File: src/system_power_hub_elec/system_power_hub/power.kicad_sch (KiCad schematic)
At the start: 37 parts, among them J1 XT90M, U220 MP2459GJ-Z-MS, U230 AP62200TWU, U240 HX4002

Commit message: Draft SPM PCB layout
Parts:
- J1: value XT90M -> XT60M; footprint Connector_AMASS:AMASS_XT90PW-M_1x02_P10.90mm_Horizontal -> Connector_AMASS:AMASS_XT60IPW-M_1x03_P7.20mm_Horizontal
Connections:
- net GND: now also J1.1 (Pin_1); no longer J1.2 (Pin_2)
- net VBUS: now also J1.2 (Pin_2); no longer J1.1 (Pin_1)
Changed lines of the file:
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@@
 	(symbol
 		(lib_id "Connector:Conn_01x02_Pin")
-		(at 30.48 29.21 0)
+		(at 30.48 31.75 0)
+		(mirror x)
 		(unit 1)
 		(exclude_from_sim no)
@@
 		(dnp no)
 		(property "Reference" "J1"
-			(at 27.178 29.21 0)
+			(at 27.178 31.75 0)
 			(effects
 				(font
@@
 			)
 		)
-		(property "Value" "XT90M"
-			(at 25.908 32.512 0)
+		(property "Value" "XT60M"
+			(at 25.908 28.448 0)
 			(effects
 				(font
@@
 			)
 		)
-		(property "Footprint" "Connector_AMASS:AMASS_XT90PW-M_1x02_P10.90mm_Horizontal"
-			(at 30.48 29.21 0)
+		(property "Footprint" "Connector_AMASS:AMASS_XT60IPW-M_1x03_P7.20mm_Horizontal"
+			(at 30.48 31.75 0)
 			(effects
 				(font
@@
 		)
 		(property "Datasheet" "~"
-			(at 30.48 29.21 0)
+			(at 30.48 31.75 0)
 			(effects
 				(font
@@
 		)
 		(property "Description" "Generic connector, single row, 01x02, script generated"
-			(at 30.48 29.21 0)
+			(at 30.48 31.75 0)
 			(effects
 				(font

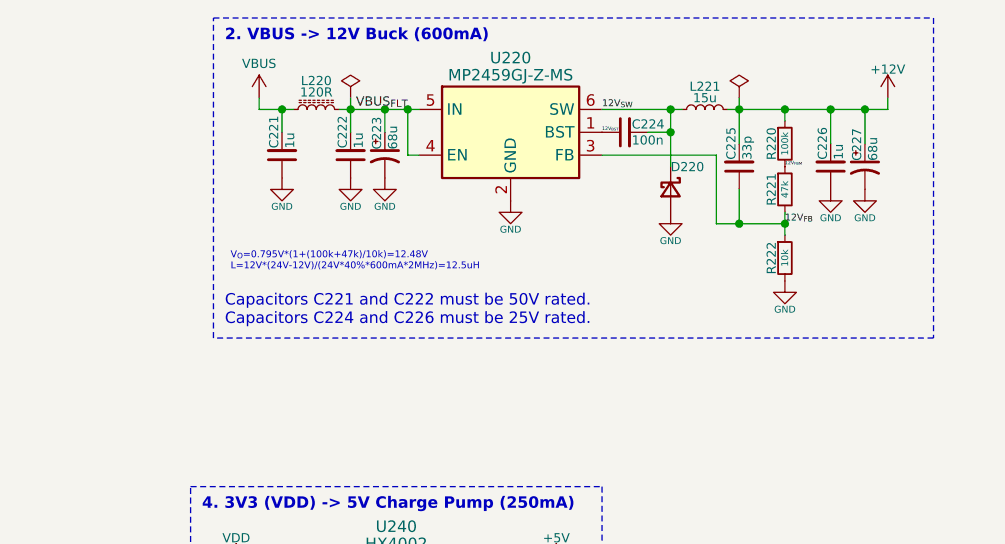
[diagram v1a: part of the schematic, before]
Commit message: Fixed XT connector routing, rewired power stuff (attempted to), made board smaller, more routing/layout progress
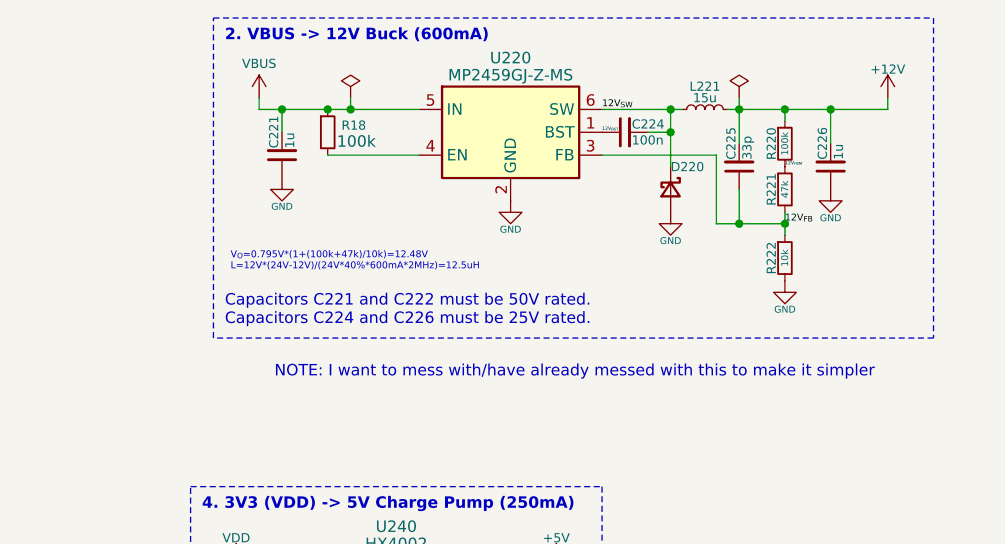
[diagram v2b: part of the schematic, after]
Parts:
- removed C222: 1u, Capacitor_SMD:C_1206_3216Metric, symbol Bluesat:C_CompactV
- removed C223, C227: 68u, Capacitor_SMD:CP_Elec_6.3x7.7, symbol Device:C_Polarized_Small_US
- removed L220: 120R, Resistor_SMD:R_0603_1608Metric, symbol Device:L_Ferrite_Small
- added R18: 100k, Resistor_SMD:R_0402_1005Metric, symbol Device:R_Small
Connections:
- net VBUS: now also U220.5 (IN), R18.1
- net VBUS_{FLT}: no longer names the net of U220.4 (EN)
- net VBUS_{FLT}: now also R18.2; no longer U220.5 (IN)
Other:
- note added: "NOTE: I want to mess with/have already messed with this to make it simpler"

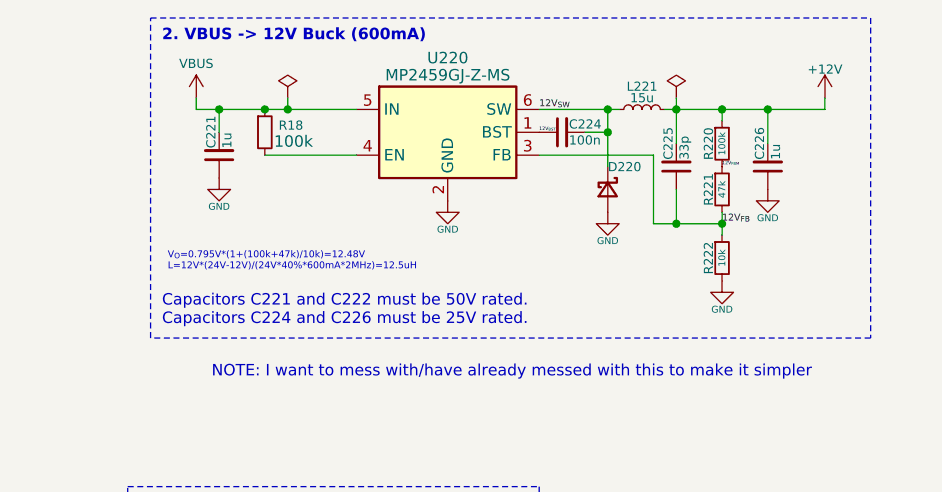
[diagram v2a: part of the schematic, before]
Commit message: Draft layout done, need to continue routing and decide on GPIO
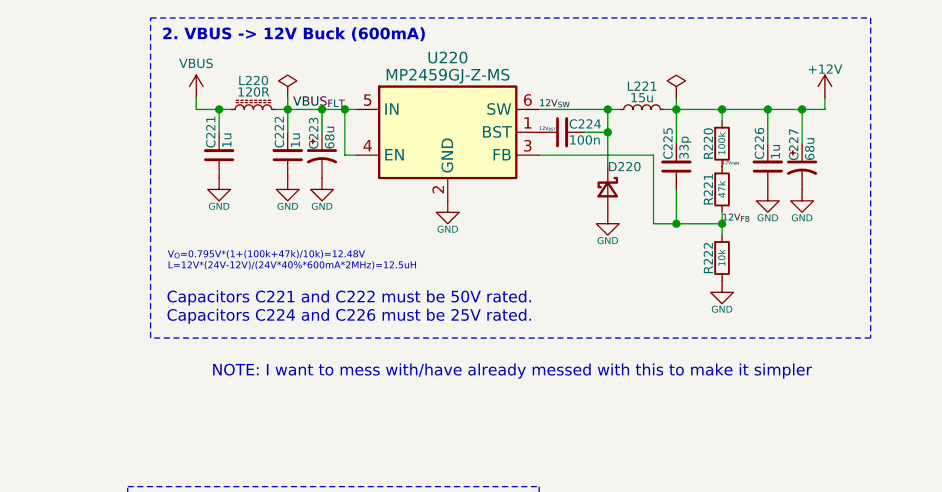
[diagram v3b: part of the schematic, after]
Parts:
- removed R18: 100k, Resistor_SMD:R_0402_1005Metric, symbol Device:R_Small
- added C222: 1u, Capacitor_SMD:C_1206_3216Metric, symbol Bluesat:C_CompactV
- added C223, C227: 68u, Capacitor_SMD:CP_Elec_6.3x7.7, symbol Device:C_Polarized_Small_US
- added L220: 120R, Resistor_SMD:R_0603_1608Metric, symbol Device:L_Ferrite_Small
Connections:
- net +12V: now also C227.1
- net GND: now also C222.1, C223.2, C227.2
- net VBUS: now also L220.1; no longer U220.5 (IN)
- net VBUS_{FLT}: now reaches U220.4 (EN)
- net VBUS_{FLT}: now also U220.5 (IN), C222.2, C223.1, L220.2

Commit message: Finish layout
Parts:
- removed C221: 1u, Capacitor_SMD:C_1206_3216Metric, symbol Bluesat:C_CompactV
- removed C223: 68u, Capacitor_SMD:CP_Elec_6.3x7.7, symbol Device:C_Polarized_Small_US
- removed L220: 120R, Resistor_SMD:R_0603_1608Metric, symbol Device:L_Ferrite_Small
- added D703, D704: SBR0560S1-7, Diode_SMD:D_SOD-882, symbol Device:D_Schottky
- C703: renamed from C222; value 1u -> 4u7; footprint Capacitor_SMD:C_1206_3216Metric -> Capacitor_SMD:C_1210_3225Metric
- J701: renamed from J1; footprint Connector_AMASS:AMASS_XT60IPW-M_1x03_P7.20mm_Horizontal -> Connector_AMASS:AMASS_XT60PW-M_1x02_P7.20mm_Horizontal
- renumbered C224 to C701, C225 to C705, C226 to C706, C227 to C707, C12 to C708, C231 to C709, C240 to C710, C242 to C711, C230 to C712, C241 to C713, C232 to C714, C233 to C715, C250 to C716, C251 to C717, C260 to C718, C261 to C719, D3 to D701, D220 to D702, L221 to L702, L230 to L703, L250 to L704, R220 to R701, R3 to R702, R221 to R703, R4 to R704, R222 to R705, R230 to R706, R231 to R707, R232 to R708, U220 to U701, U230 to U702, U240 to U703
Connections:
- net VBUS_{FLT} is gone; now on net VBUS: C703.2, U701.4 (EN), U701.5 (IN)
- net +12V: now also D703.2 (A), D704.1 (K)
- net VBUS: now also D703.1 (K)
- net VDD: now also D704.2 (A)
